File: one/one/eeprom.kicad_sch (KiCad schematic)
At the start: 0 parts

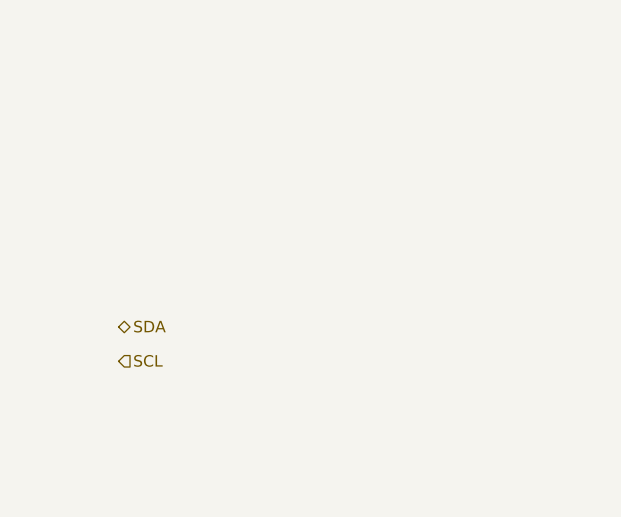
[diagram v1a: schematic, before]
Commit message: add EEPROM, remove one mounting hole
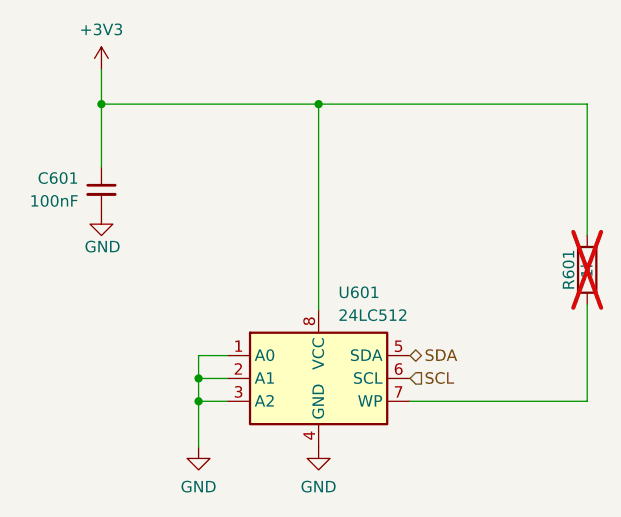
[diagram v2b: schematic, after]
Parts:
- added C601: 100nF, Capacitor_SMD:C_0603_1608Metric, symbol Device:C_Small
- added R601: 1k, Resistor_SMD:R_0603_1608Metric, symbol Device:R
- added U601: 24LC512, Package_DFN_QFN:DFN-8-1EP_3x2mm_P0.5mm_EP1.7x1.4mm, symbol Memory_EEPROM:24LC512
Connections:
- net SCL: now also U601.6 (SCL)
- net SDA: now also U601.5 (SDA)
- new net: R601.1, U601.7 (WP)
- new net +3V3: C601.1, R601.2, U601.8 (VCC)
- new net GND: C601.2, U601.1 (A0), U601.2 (A1), U601.3 (A2), U601.4 (GND)
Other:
- company: (none) -> ${LINK}

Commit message: add vendor links
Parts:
- C601: Digikey (none) -> https://www.digikey.de/en/products/detail/cal-chip-electron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; MPN (none) -> GMC10X7R104K50NT
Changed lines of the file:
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@@
 	(title_block
 		(title "${TITLE}")
-		(date "2025-01-06")
+		(date "2025-01-26")
 		(rev "${REVISION}")
 		(company "${LINK}")
@@
 			)
 		)
-		(property "Datasheet" "~"
+		(property "Datasheet" "https://calchip.com/wp-content/uploads/2023/09/GMC-Series-2.pdf"
 			(at 127 68.58 0)
 			(effects
@@
 			)
 		)
-		(property "Description" "Unpolarized capacitor, small symbol"
+		(property "Description" "0.1 µF ±10% 50V Ceramic Capacitor X7R 0603 (1608 Metric)"
 			(at 127 68.58 0)
 			(effects
@@
 			)
 		)
-		(property "MPN" ""
+		(property "MPN" "GMC10X7R104K50NT"
 			(at 127 68.58 0)
 			(effects
@@
 			)
 		)
-		(property "Digikey" ""
+		(property "Digikey" "https://www.digikey.de/en/products/detail/cal-chip-electronics-inc/GMC10X7R104K50NT/18151094"
 			(at 127 68.58 0)
 			(effects
